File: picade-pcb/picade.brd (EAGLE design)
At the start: 76 x 50 mm, 60 parts, among them P1JOY 2.54MM-5P-SCREW-TERMINALLOCK, P2JOY 2.54MM-5P-SCREW-TERMINALLOCK

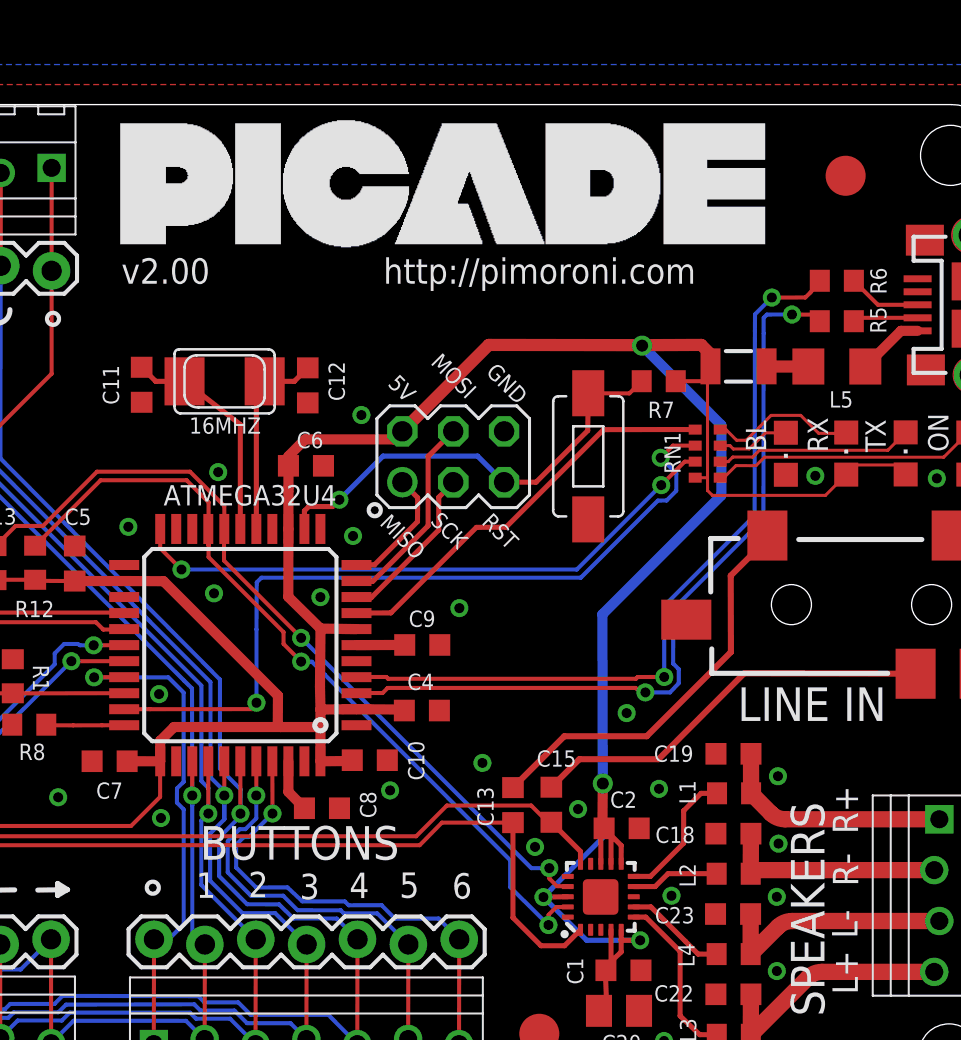
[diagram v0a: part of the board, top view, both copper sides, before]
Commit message: Minor aesthetic changes
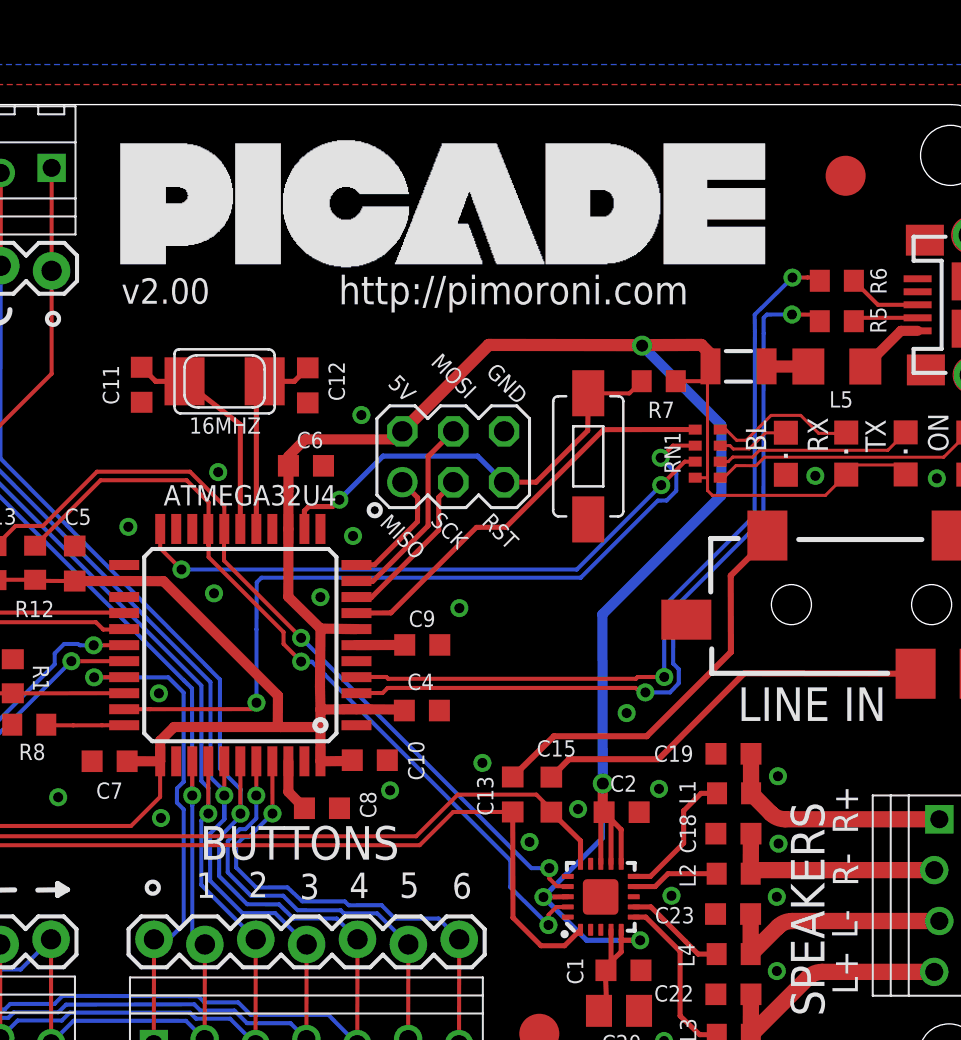
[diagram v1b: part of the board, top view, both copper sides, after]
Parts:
- moved C2 0.80 mm to (57.0, 14.7)
- moved C13 0.53 mm to (51.6, 15.6)
- moved C15 0.50 mm to (53.5, 15.5)
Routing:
- net 5V: track 178.6 -> 180.1 mm
- net LINEINR: track 61.1 -> 62.0 mm
- net LINEINL: track 54.0 -> 54.7 mm

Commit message: Picade retail board V2.01
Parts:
- U$1, U$2, U$3: value FIDUCIAL2MM -> FIDUCIAL1MM; device pimoroni:FIDUCIAL-2MM -> pimoroni:FIDUCIAL-1MM
- U$5: device pimoroni:QFN20 -> pimoroni:TPA2016
- moved U$1 47.0 mm to (69.3, 47.7)
- moved U$2 44.1 mm to (69.3, 2.39)
- moved U$3 12.9 mm to (7.11, 25.0)
- moved C2 0.85 mm to (57.0, 15.5)
- moved R13 0.43 mm to (26.2, 27.0)
- moved R12 0.43 mm to (28.1, 27.0)
- moved C5 0.30 mm to (30.0, 27.0)
- moved C20 0.11 mm to (57.0, 4.73)
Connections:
- net MODESHIFT: now also ATMEGA32U4.25
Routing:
- net MODESHIFT: track 4.63 -> 39.8 mm, vias 0 -> 1
- net OUTR-: track 4.41 -> 3.73 mm
- net OUTR+: track 6.83 -> 6.15 mm
- net 5V: track 180.1 -> 180.7 mm
- net SCL: track 40.6 -> 40.0 mm
- net OUTL-: track 5.12 -> 4.60 mm
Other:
- board text added: "+L-"
- board text added: "-R+"
- board text added: "v2.01"
- board text removed: "L+"
- board text removed: "L-"
- board text removed: "R+"
- board text removed: "R-"
- board text removed: "http://pimoroni.com"

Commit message: Prior to amplifier change
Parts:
- C20: value (none) -> 10uF
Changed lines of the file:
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@@
 <layer number="20" name="Dimension" color="15" fill="1" visible="yes" active="yes"/>
 <layer number="21" name="tPlace" color="7" fill="1" visible="yes" active="yes"/>
-<layer number="22" name="bPlace" color="7" fill="1" visible="yes" active="yes"/>
+<layer number="22" name="bPlace" color="7" fill="1" visible="no" active="yes"/>
 <layer number="23" name="tOrigins" color="15" fill="1" visible="yes" active="yes"/>
 <layer number="24" name="bOrigins" color="15" fill="1" visible="yes" active="yes"/>
@@
 </class>
 </classes>
-<designrules name="default *">
-<description language="de">&lt;b&gt;EAGLE Design Rules&lt;/b&gt;
-&lt;p&gt;
-Die Standard-Design-Rules sind so gewählt, dass sie für
-die meisten Anwendungen passen. Sollte ihre Platine
-besondere Anforderungen haben, treffen Sie die erforderlichen
-Einstellungen hier und speichern die Design Rules unter
-einem neuen Namen ab.</description>
+<designrules name="pimoroni">
 <description language="en">&lt;b&gt;EAGLE Design Rules&lt;/b&gt;
 &lt;p&gt;
@@
 <param name="mnLayersViaInSmd" value="2"/>
 <param name="mdCopperDimension" value="20mil"/>
-<param name="mdDrill" value="8mil"/>
+<param name="mdDrill" value="6mil"/>
 <param name="mdSmdStop" value="0mil"/>
-<param name="msWidth" value="6mil"/>
-<param name="msDrill" value="18mil"/>
+<param name="msWidth" value="8mil"/>
+<param name="msDrill" value="12mil"/>
 <param name="msMicroVia" value="9.99mm"/>
 <param name="msBlindViaRatio" value="0.5"/>
@@
 <param name="rvMicroViaOuter" value="0.25"/>
 <param name="rvMicroViaInner" value="0.25"/>
-<param name="rlMinPadTop" value="10mil"/>
+<param name="rlMinPadTop" value="12mil"/>
 <param name="rlMaxPadTop" value="20mil"/>
 <param name="rlMinPadInner" value="10mil"/>
 <param name="rlMaxPadInner" value="20mil"/>
-<param name="rlMinPadBottom" value="10mil"/>
+<param name="rlMinPadBottom" value="12mil"/>
 <param name="rlMaxPadBottom" value="20mil"/>
-<param name="rlMinViaOuter" value="8mil"/>
+<param name="rlMinViaOuter" value="10mil"/>
 <param name="rlMaxViaOuter" value="20mil"/>
-<param name="rlMinViaInner" value="8mil"/>
+<param name="rlMinViaInner" value="10mil"/>
 <param name="rlMaxViaInner" value="20mil"/>
 <param name="rlMinMicroViaOuter" value="4mil"/>
@@
 <param name="mvStopFrame" value="1"/>
 <param name="mvCreamFrame" value="0"/>
-<param name="mlMinStopFrame" value="4mil"/>
-<param name="mlMaxStopFrame" value="4mil"/>
+<param name="mlMinStopFrame" value="1mil"/>
+<param name="mlMaxStopFrame" value="1mil"/>
 <param name="mlMinCreamFrame" value="0mil"/>
 <param name="mlMaxCreamFrame" value="0mil"/>
@@
 <attribute name="NAME" x="59.97" y="31.567" size="0.8128" layer="25" font="vector" ratio="14" rot="R90"/>
 </element>
-<element name="C20" library="resistor" package="C0805K" value="" x="56.997" y="4.728" smashed="yes">
+<element name="C20" library="resistor" package="C0805K" value="10uF" x="56.997" y="4.728" smashed="yes">
 <attribute name="NAME" x="58.085" y="3.471" size="0.8128" layer="25" font="vector" ratio="14" rot="R180"/>
 <attribute name="VALUE" x="55.997" y="2.828" size="1.016" layer="27"/>

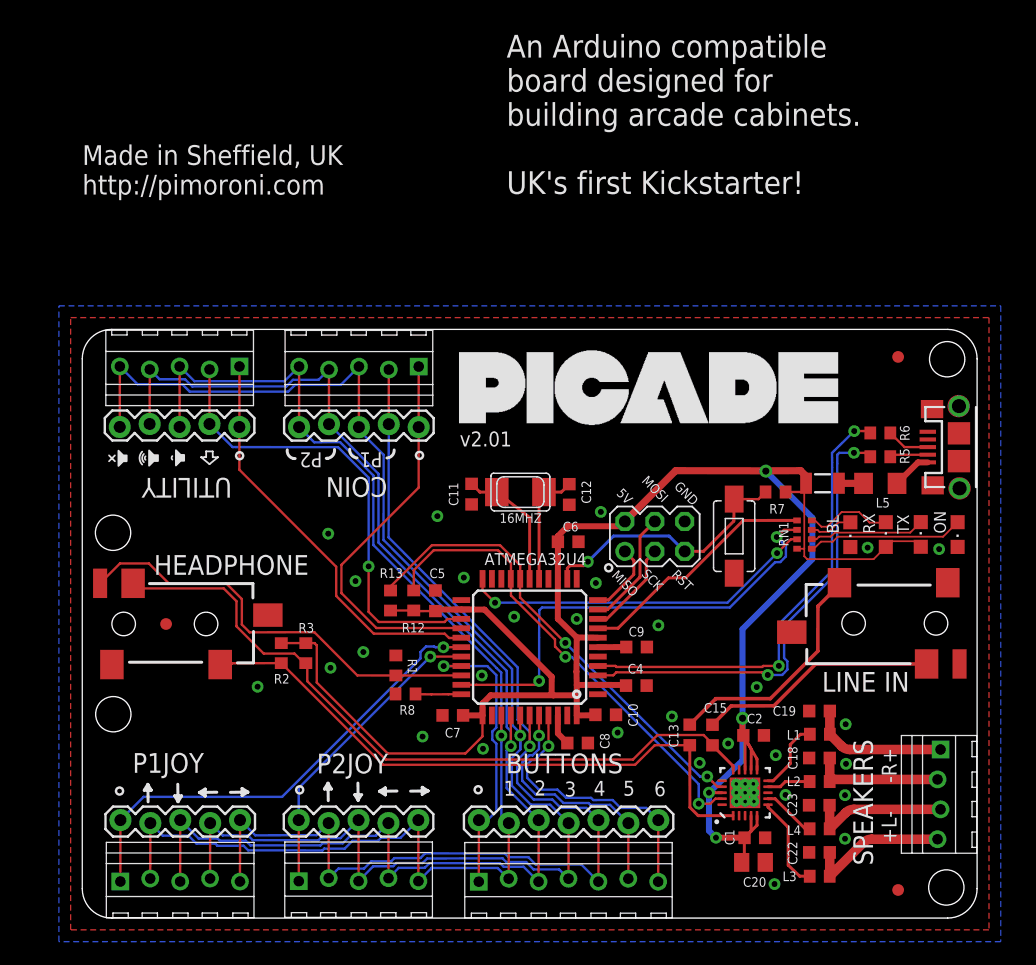
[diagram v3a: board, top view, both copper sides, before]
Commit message: v1.02
Changed amp to allow for up/down volume control. Better USB signal
routing. Pull-up on MODESHIFT
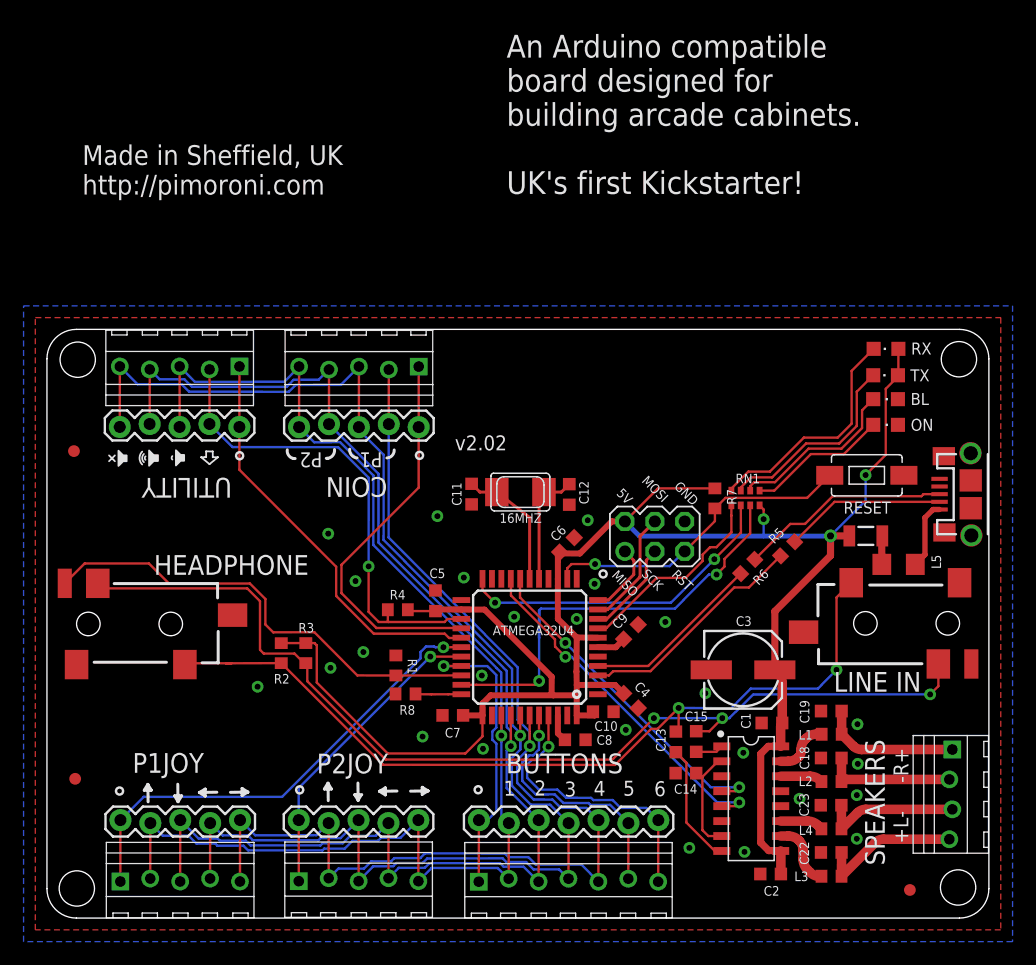
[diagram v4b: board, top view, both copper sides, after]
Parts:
- removed C20: 10uF, resistor:C0805K
- removed R12, R13: 4.7KR, resistor:R0603
- removed U$5: TPA2016, pimoroni:TPA2016
- added C14: 0.1uF, resistor:C0603K
- added C3: 100uF, resistor:153CLV-0605
- added R4: 47KR, resistor:R0603
- added U$4: PAM8407, pimoroni:SO-16
- C13, C15: value 1uF -> 0.1uF
- moved U$1 70.5 mm to (-0.72, 39.7)
- moved R6 16.0 mm to (56.5, 29.9), turned to 225 degrees
- moved RX 15.8 mm to (68.3, 48.3), turned to 90 degrees
- moved U$3 15.2 mm to (-0.61, 11.8)
- moved TX 13.8 mm to (68.2, 46.1), turned to 90 degrees
- moved RESET 12.4 mm to (66.6, 37.6), turned to 0 degrees
- moved BL 11.9 mm to (68.2, 44.1), turned to 270 degrees
- moved C2 11.9 mm to (58.5, 3.75), turned to 180 degrees
- moved ON 11.1 mm to (68.2, 41.9), turned to 270 degrees
- moved R5 11.1 mm to (59.9, 31.4), turned to 225 degrees
- moved C1 9.86 mm to (58.6, 16.6), turned to 180 degrees
- moved L5 7.05 mm to (69.3, 30.0)
- moved RN1 5.89 mm to (56.3, 35.7), turned to 180 degrees
- moved F1 5.79 mm to (66.5, 32.5)
- moved R7 5.18 mm to (53.7, 35.6), turned to 270 degrees
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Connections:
- removed net PRELINEINL: C13.1, LINEIN.TIP
- removed net PRELINEINR: C15.1, LINEIN.RING
- removed net SCL: ATMEGA32U4.18, R13.1, U$5.21
- removed net SDA: ATMEGA32U4.19, R12.1, U$5.23
- new net LIENINLCAP: C13.2, U$4.8
- new net LINEINRCAP: C15.2, U$4.1
- new net N$9: C14.2, U$4.2, U$4.7
- new net SHDWN: U$4.3
- new net VDOWN: ATMEGA32U4.19, U$4.5
- new net VUP: ATMEGA32U4.18, U$4.4
- net 5V: now also C3.+, R4.2, U$4.16, U$4.9; no longer C20.1, R12.2, R13.2, U$5.14, U$5.15, U$5.16, U$5.22, U$5.4, U$5.5
- net BLLED: now also RN1.7; no longer RN1.6
- net GND: now also C14.1, C3.-, U$4.12, U$4.13, U$4.6; no longer C20.2, U$5.17, U$5.2, U$5.3, U$5.9, U$5.GND
- net LINEINL: now also C13.1, LINEIN.TIP; no longer C13.2, U$5.1
- net LINEINR: now also C15.1, LINEIN.RING; no longer C15.2, U$5.18
- net MODESHIFT: now also R4.1
- net N$11: now also RN1.3; no longer RN1.2
- net N$6: now also RN1.2; no longer RN1.3
- net OUTL+: now also U$4.10; no longer U$5.7
- net OUTL-: now also U$4.11; no longer U$5.8
- net OUTR+: now also U$4.15; no longer U$5.11
- net OUTR-: now also U$4.14; no longer U$5.10
- net TXLED: now also RN1.6; no longer RN1.7
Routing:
- net SDA: track 41.5 -> 0.00 mm, vias 2 -> 0
- net SCL: track 40.0 -> 0.00 mm, vias 2 -> 0
- net VDOWN: track 0.00 -> 30.1 mm, vias 0 -> 2
- net VUP: track 0.00 -> 28.5 mm, vias 0 -> 2
- net LINEINR: track 61.6 -> 88.0 mm, vias 0 -> 3
- net D+: track 39.5 -> 15.4 mm, vias 2 -> 0
- net PRELINEINR: track 20.3 -> 0.00 mm
- net PRELINEINL: track 20.0 -> 0.00 mm
- net D-: track 39.7 -> 19.7 mm, vias 2 -> 0
- net LINEINL: track 54.4 -> 73.6 mm, vias 0 -> 2
- net 5V: track 180.7 -> 165.2 mm, vias 4 -> 3
- net N$4: track 3.68 -> 18.0 mm
- net N$12: track 7.40 -> 19.8 mm
- net N$6: track 3.68 -> 14.8 mm
- net N$3: track 3.25 -> 13.7 mm
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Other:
- board size 76 x 50 mm -> 80 x 50 mm
- board text added: "RESET"
- board text added: "v2.02"
- board text removed: "v2.01"
